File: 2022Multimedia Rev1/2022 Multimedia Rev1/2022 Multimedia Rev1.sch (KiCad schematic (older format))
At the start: 31 parts

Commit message: neatened up schematic
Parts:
- gave numbers to parts that had none: 22
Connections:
- wire segments 86 -> 90
- no-connect marks 0 -> 70
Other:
- moved on the sheet: C3, C6, C7, Conn2, Conn3, Conn4, Conn5, Conn6, R3

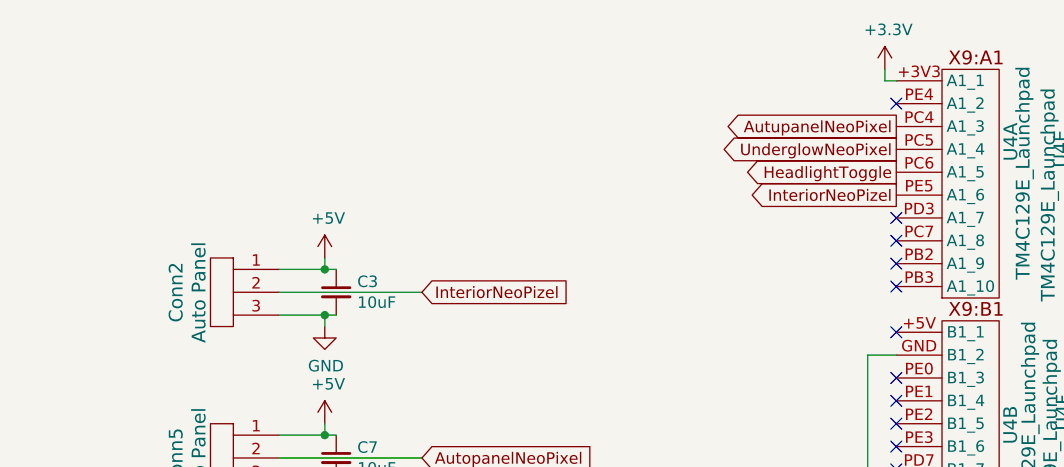
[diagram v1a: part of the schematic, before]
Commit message: Added another neopixel
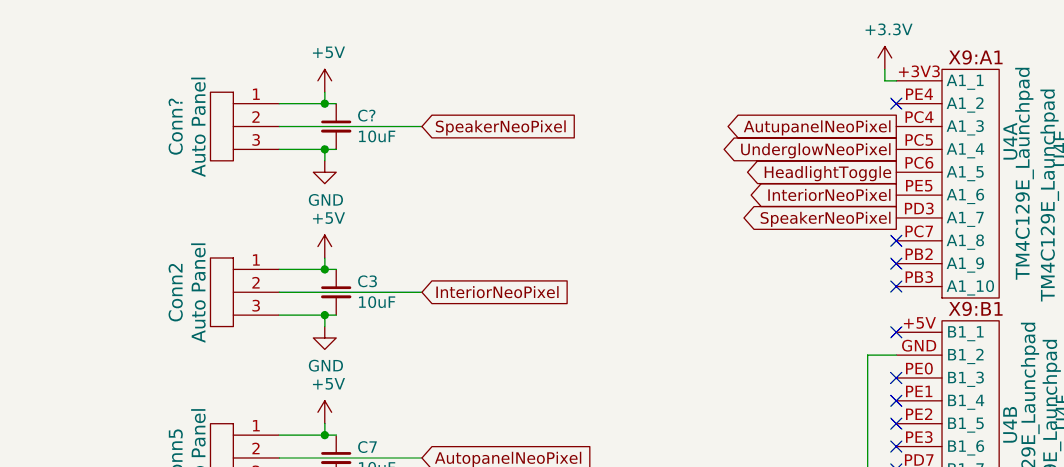
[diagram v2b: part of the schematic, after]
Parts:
- added C?: 10uF, symbol Device:C_Small
- added Conn?: Auto Panel, MRDT_Connectors:MOLEX_uF_S_03_Horizontal, symbol MRDT_Connectors:Molex_uF_S_03
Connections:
- net labels added: InteriorNeoPixel, SpeakerNeoPixel
- net labels removed: InteriorNeoPizel
- wire segments 90 -> 97
- no-connect marks 70 -> 69
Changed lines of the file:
@@
 	6700 1800 6500 1800
 Text GLabel 7125 1900 2    50   Input ~ 0
-InteriorNeoPizel
+InteriorNeoPixel
 Text GLabel 9200 1475 0    50   Output ~ 0
-InteriorNeoPizel
+InteriorNeoPixel
 Wire Wire Line
 	6500 3200 6650 3200
@@
 NoConn ~ 10425 1075
 NoConn ~ 9200 1075
-NoConn ~ 9200 1575
 NoConn ~ 9200 1675
 NoConn ~ 9200 1775
 NoConn ~ 9200 1875
+$Comp
+L MRDT_Connectors:Molex_uF_S_03 Conn?
+U 1 1 6166808D
+P 6300 1325
+F 0 "Conn?" V 6550 1475 60  0000 C CNN
+F 1 "Auto Panel" V 6450 1475 60  0000 C CNN
+F 2 "MRDT_Connectors:MOLEX_uF_S_03_Horizontal" H 6300 1325 60  0001 C CNN
+F 3 "" H 6300 1325 60  0001 C CNN
+	1    6300 1325
+	-1   0    0    -1
+$EndComp
+$Comp
+L Device:C_Small C?
+U 1 1 61668093
+P 6750 1175
+F 0 "C?" H 6842 1221 50  0000 L CNN
+F 1 "10uF" H 6842 1130 50  0000 L CNN
+F 2 "" H 6750 1175 50  0001 C CNN
+F 3 "~" H 6750 1175 50  0001 C CNN
+	1    6750 1175
+	1    0    0    -1
+$EndComp
+$Comp
+L power:GND #PWR?
+U 1 1 61668099
+P 6700 1325
+F 0 "#PWR?" H 6700 1075 50  0001 C CNN
+F 1 "GND" H 6705 1152 50  0000 C CNN
+F 2 "" H 6700 1325 50  0001 C CNN
+F 3 "" H 6700 1325 50  0001 C CNN
+	1    6700 1325
+	1    0    0    -1
+$EndComp
+$Comp
+L power:+5V #PWR?
+U 1 1 6166809F
+P 6700 1025
+F 0 "#PWR?" H 6700 875 50  0001 C CNN
+F 1 "+5V" H 6715 1198 50  0000 C CNN
+F 2 "" H 6700 1025 50  0001 C CNN
+F 3 "" H 6700 1025 50  0001 C CNN
+	1    6700 1025
+	1    0    0    -1
+$EndComp
+Wire Wire Line
+	6700 1325 6700 1275
+Wire Wire Line
+	6500 1275 6700 1275
+Wire Wire Line
+	6750 1075 6700 1075
+Wire Wire Line
+	6700 1025 6700 1075
+Connection ~ 6700 1275
+Wire Wire Line
+	6700 1275 6750 1275
+Connection ~ 6700 1075
+Wire Wire Line
+	6700 1075 6500 1075
+Text GLabel 7125 1175 2    50   Input ~ 0
+SpeakerNeoPixel
+Wire Wire Line
+	6500 1175 7125 1175
+Text GLabel 9200 1575 0    50   Output ~ 0
+SpeakerNeoPixel
 $EndSCHEMATC

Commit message: Fin
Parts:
- R1: value 330 -> 47
- R2: value 480 -> 100
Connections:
- wire segments 97 -> 102
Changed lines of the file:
@@
 P 4750 2875
 F 0 "R1" V 4925 2875 50  0000 C CNN
-F 1 "330" V 4850 2875 50  0000 C CNN
+F 1 "47" V 4850 2875 50  0000 C CNN
 F 2 "" H 4750 2875 50  0001 C CNN
 F 3 "~" H 4750 2875 50  0001 C CNN
@@
 P 4750 3750
 F 0 "R2" V 4925 3750 50  0000 C CNN
-F 1 "480" V 4850 3750 50  0000 C CNN
+F 1 "100" V 4850 3750 50  0000 C CNN
 F 2 "" H 4750 3750 50  0001 C CNN
 F 3 "~" H 4750 3750 50  0001 C CNN
@@
 	9075 4275 9075 4375
 Wire Wire Line
-	9075 2175 9075 4275
-Wire Wire Line
 	9075 2175 9200 2175
 Connection ~ 9075 4275
@@
 Text GLabel 7125 2625 2    50   Input ~ 0
 AutopanelNeoPixel
-Text GLabel 9200 1175 0    50   Output ~ 0
+Text GLabel 8950 2675 0    50   Output ~ 0
 AutupanelNeoPixel
-Text GLabel 9200 1275 0    50   Output ~ 0
+Text GLabel 8950 2775 0    50   Output ~ 0
 UnderglowNeoPixel
-Text GLabel 9200 1375 0    50   Output ~ 0
+Text GLabel 8950 2575 0    50   Output ~ 0
 HeadlightToggle
 $Comp
@@
 Text GLabel 7125 1900 2    50   Input ~ 0
 InteriorNeoPixel
-Text GLabel 9200 1475 0    50   Output ~ 0
+Text GLabel 8950 2975 0    50   Output ~ 0
 InteriorNeoPixel
 Wire Wire Line
@@
 NoConn ~ 9200 2375
 NoConn ~ 9200 2475
-NoConn ~ 9200 2575
-NoConn ~ 9200 2675
-NoConn ~ 9200 2775
-NoConn ~ 9200 2875
-NoConn ~ 9200 2975
 NoConn ~ 10425 1875
 NoConn ~ 10425 1775
@@
 Wire Wire Line
 	6500 1175 7125 1175
-Text GLabel 9200 1575 0    50   Output ~ 0
+Text GLabel 8950 2875 0    50   Output ~ 0
 SpeakerNeoPixel
+NoConn ~ 9200 1175
+NoConn ~ 9200 1275
+NoConn ~ 9200 1375
+NoConn ~ 9200 1475
+NoConn ~ 9200 1575
+Wire Wire Line
+	9075 2175 9075 4275
+Wire Wire Line
+	9200 2575 8950 2575
+Wire Wire Line
+	8950 2675 9200 2675
+Wire Wire Line
+	9200 2775 8950 2775
+Wire Wire Line
+	8950 2875 9200 2875
+Wire Wire Line
+	9200 2975 8950 2975
 $EndSCHEMATC

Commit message: finished layout
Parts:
- C1, C2, C3, C4, C5, C6, C7: footprint (none) -> Capacitor_SMD:C_0603_1608Metric_Pad1.05x0.95mm_HandSolder
- C8: renamed from C?; footprint (none) -> Capacitor_SMD:C_0603_1608Metric_Pad1.05x0.95mm_HandSolder
- Conn1: footprint (none) -> MRDT_Connectors:Anderson_3_Horizontal_Side_by_Side
- Conn2: value Auto Panel -> Interior Lights
- Conn7: renamed from Conn?; value Auto Panel -> Speaker Panel
- D1, D2: footprint (none) -> Diode_SMD:D_0603_1608Metric_Pad1.05x0.95mm_HandSolder
- R1, R2, R3: footprint (none) -> Resistor_SMD:R_0603_1608Metric_Pad1.05x0.95mm_HandSolder
- U1, U2: footprint (none) -> MRDT_Devices:OKI_Horizontal
- U3: footprint (none) -> Package_SO:SOIC-8-1EP_3.9x4.9mm_P1.27mm_EP2.29x3mm
- U4: footprint (none) -> MRDT_Shields:TM4C129E_Launchpad_FULL_SMD_BOTTOM
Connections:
- net labels removed: AutupanelNeoPixel
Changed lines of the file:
@@
 F 0 "U4" V 9701 2523 60  0000 L CNN
 F 1 "TM4C129E_Launchpad" V 9755 2005 60  0000 L CNN
-F 2 "" H 9400 1925 60  0001 C CNN
+F 2 "MRDT_Shields:TM4C129E_Launchpad_FULL_SMD_BOTTOM" H 9400 1925 60  0001 C CNN
 F 3 "" H 9400 1925 60  0001 C CNN
 	1    9400 1925
@@
 F 0 "U4" V 9700 3485 60  0000 L CNN
 F 1 "TM4C129E_Launchpad" V 9780 3090 60  0000 L CNN
-F 2 "" H 9400 3025 60  0001 C CNN
+F 2 "MRDT_Shields:TM4C129E_Launchpad_FULL_SMD_BOTTOM" H 9400 3025 60  0001 C CNN
 F 3 "" H 9400 3025 60  0001 C CNN
 	2    9400 3025
@@
 F 0 "U4" V 9695 4665 60  0000 L CNN
 F 1 "TM4C129E_Launchpad" V 9755 4135 60  0000 L CNN
-F 2 "" H 9400 4125 60  0001 C CNN
+F 2 "MRDT_Shields:TM4C129E_Launchpad_FULL_SMD_BOTTOM" H 9400 4125 60  0001 C CNN
 F 3 "" H 9400 4125 60  0001 C CNN
 	3    9400 4125
@@
 F 0 "U4" V 9695 5765 60  0000 L CNN
 F 1 "TM4C129E_Launchpad" V 9755 5225 60  0000 L CNN
-F 2 "" H 9400 5225 60  0001 C CNN
+F 2 "MRDT_Shields:TM4C129E_Launchpad_FULL_SMD_BOTTOM" H 9400 5225 60  0001 C CNN
 F 3 "" H 9400 5225 60  0001 C CNN
 	4    9400 5225
@@
 F 0 "U4" V 10530 2495 60  0000 L CNN
 F 1 "TM4C129E_Launchpad" V 10585 1910 60  0000 L CNN
-F 2 "" H 10225 1925 60  0001 C CNN
+F 2 "MRDT_Shields:TM4C129E_Launchpad_FULL_SMD_BOTTOM" H 10225 1925 60  0001 C CNN
 F 3 "" H 10225 1925 60  0001 C CNN
 	5    10225 1925
@@
 F 0 "U4" V 10520 3545 60  0000 L CNN
 F 1 "TM4C129E_Launchpad" V 10575 3015 60  0000 L CNN
-F 2 "" H 10225 3025 60  0001 C CNN
+F 2 "MRDT_Shields:TM4C129E_Launchpad_FULL_SMD_BOTTOM" H 10225 3025 60  0001 C CNN
 F 3 "" H 10225 3025 60  0001 C CNN
 	6    10225 3025
@@
 F 0 "U4" V 10525 4770 60  0000 L CNN
 F 1 "TM4C129E_Launchpad" V 10580 4220 60  0000 L CNN
-F 2 "" H 10225 4125 60  0001 C CNN
+F 2 "MRDT_Shields:TM4C129E_Launchpad_FULL_SMD_BOTTOM" H 10225 4125 60  0001 C CNN
 F 3 "" H 10225 4125 60  0001 C CNN
 	7    10225 4125
@@
 F 0 "U4" V 10520 5815 60  0000 L CNN
 F 1 "TM4C129E_Launchpad" V 10570 5275 60  0000 L CNN
-F 2 "" H 10225 5225 60  0001 C CNN
+F 2 "MRDT_Shields:TM4C129E_Launchpad_FULL_SMD_BOTTOM" H 10225 5225 60  0001 C CNN
 F 3 "" H 10225 5225 60  0001 C CNN
 	8    10225 5225
@@
 F 0 "Conn1" H 1500 3900 60  0000 C CNN
 F 1 "AndersonPP" H 1400 3825 60  0000 C CNN
-F 2 "" H 1525 3200 60  0001 C CNN
+F 2 "MRDT_Connectors:Anderson_3_Horizontal_Side_by_Side" H 1525 3200 60  0001 C CNN
 F 3 "" H 1525 3200 60  0001 C CNN
 	1    1675 3750
@@
 F 0 "U1" H 4000 2925 60  0001 C CNN
 F 1 "OKI" H 4150 3256 60  0000 C CNN
-F 2 "" H 3750 2875 60  0001 C CNN
+F 2 "MRDT_Devices:OKI_Horizontal" H 3750 2875 60  0001 C CNN
 F 3 "" H 3750 2875 60  0001 C CNN
 	1    3950 2975
@@
 F 0 "C1" H 3792 3071 50  0000 L CNN
 F 1 "10 uF" H 3792 2980 50  0000 L CNN
-F 2 "" H 3700 3025 50  0001 C CNN
+F 2 "Capacitor_SMD:C_0603_1608Metric_Pad1.05x0.95mm_HandSolder" H 3700 3025 50  0001 C CNN
 F 3 "~" H 3700 3025 50  0001 C CNN
 	1    3700 3025
@@
 F 0 "C4" H 4425 3050 50  0000 L CNN
 F 1 "10 uF" H 4300 2975 50  0000 L CNN
-F 2 "" H 4600 3025 50  0001 C CNN
+F 2 "Capacitor_SMD:C_0603_1608Metric_Pad1.05x0.95mm_HandSolder" H 4600 3025 50  0001 C CNN
 F 3 "~" H 4600 3025 50  0001 C CNN
 	1    4600 3025
@@
 F 0 "R1" V 4925 2875 50  0000 C CNN
 F 1 "47" V 4850 2875 50  0000 C CNN
-F 2 "" H 4750 2875 50  0001 C CNN
+F 2 "Resistor_SMD:R_0603_1608Metric_Pad1.05x0.95mm_HandSolder" H 4750 2875 50  0001 C CNN
 F 3 "~" H 4750 2875 50  0001 C CNN
 	1    4750 2875
@@
 F 0 "D1" H 5043 2620 50  0000 C CNN
 F 1 "Green" H 5043 2711 50  0000 C CNN
-F 2 "" H 5050 2875 50  0001 C CNN
+F 2 "Diode_SMD:D_0603_1608Metric_Pad1.05x0.95mm_HandSolder" H 5050 2875 50  0001 C CNN
 F 3 "~" H 5050 2875 50  0001 C CNN
 	1    5050 2875
@@
 F 0 "U2" H 4000 3800 60  0001 C CNN
 F 1 "OKI" H 4150 4131 60  0000 C CNN
-F 2 "" H 3750 3750 60  0001 C CNN
+F 2 "MRDT_Devices:OKI_Horizontal" H 3750 3750 60  0001 C CNN
 F 3 "" H 3750 3750 60  0001 C CNN
 	1    3950 3850
@@
 F 0 "C2" H 3792 3946 50  0000 L CNN
 F 1 "10 uF" H 3792 3855 50  0000 L CNN
-F 2 "" H 3700 3900 50  0001 C CNN
+F 2 "Capacitor_SMD:C_0603_1608Metric_Pad1.05x0.95mm_HandSolder" H 3700 3900 50  0001 C CNN
 F 3 "~" H 3700 3900 50  0001 C CNN
 	1    3700 3900
@@
 F 0 "C5" H 4425 3925 50  0000 L CNN
 F 1 "10 uF" H 4300 3850 50  0000 L CNN
-F 2 "" H 4600 3900 50  0001 C CNN
+F 2 "Capacitor_SMD:C_0603_1608Metric_Pad1.05x0.95mm_HandSolder" H 4600 3900 50  0001 C CNN
 F 3 "~" H 4600 3900 50  0001 C CNN
 	1    4600 3900
@@
 F 0 "R2" V 4925 3750 50  0000 C CNN
 F 1 "100" V 4850 3750 50  0000 C CNN
-F 2 "" H 4750 3750 50  0001 C CNN
+F 2 "Resistor_SMD:R_0603_1608Metric_Pad1.05x0.95mm_HandSolder" H 4750 3750 50  0001 C CNN
 F 3 "~" H 4750 3750 50  0001 C CNN
 	1    4750 3750
@@
 F 0 "D2" H 5043 3495 50  0000 C CNN
 F 1 "Green" H 5043 3586 50  0000 C CNN
-F 2 "" H 5050 3750 50  0001 C CNN
+F 2 "Diode_SMD:D_0603_1608Metric_Pad1.05x0.95mm_HandSolder" H 5050 3750 50  0001 C CNN
 F 3 "~" H 5050 3750 50  0001 C CNN
 	1    5050 3750
@@
 F 0 "Conn1" H 1500 3650 60  0000 C CNN
 F 1 "AndersonPP" H 1400 3575 60  0000 C CNN
-F 2 "" H 1525 2975 60  0001 C CNN
+F 2 "MRDT_Connectors:Anderson_3_Horizontal_Side_by_Side" H 1525 2975 60  0001 C CNN
 F 3 "" H 1525 2975 60  0001 C CNN
 	3    1675 3525
@@
 F 0 "Conn1" H 1500 3450 60  0000 C CNN
 F 1 "AndersonPP" H 1400 3375 60  0000 C CNN
-F 2 "" H 1525 2750 60  0001 C CNN
+F 2 "MRDT_Connectors:Anderson_3_Horizontal_Side_by_Side" H 1525 2750 60  0001 C CNN
 F 3 "" H 1525 2750 60  0001 C CNN
 	2    1675 3300
@@
 F 0 "C6" H 6800 3400 50  0000 L CNN
 F 1 "10 uF" H 6800 3200 50  0000 L CNN
-F 2 "" H 6700 3300 50  0001 C CNN
+F 2 "Capacitor_SMD:C_0603_1608Metric_Pad1.05x0.95mm_HandSolder" H 6700 3300 50  0001 C CNN
 F 3 "~" H 6700 3300 50  0001 C CNN
 	1    6700 3300
@@
 F 0 "C7" H 6842 2671 50  0000 L CNN
 F 1 "10uF" H 6842 2580 50  0000 L CNN
-F 2 "" H 6750 2625 50  0001 C CNN
+F 2 "Capacitor_SMD:C_0603_1608Metric_Pad1.05x0.95mm_HandSolder" H 6750 2625 50  0001 C CNN
 F 3 "~" H 6750 2625 50  0001 C CNN
 	1    6750 2625
@@
 AutopanelNeoPixel
 Text GLabel 8950 2675 0    50   Output ~ 0
-AutupanelNeoPixel
+AutopanelNeoPixel
 Text GLabel 8950 2775 0    50   Output ~ 0
 UnderglowNeoPixel
@@
 F 0 "R3" H 7143 4696 50  0000 L CNN
 F 1 "480" H 7143 4605 50  0000 L CNN
-F 2 "" H 7075 4650 50  0001 C CNN
+F 2 "Resistor_SMD:R_0603_1608Metric_Pad1.05x0.95mm_HandSolder" H 7075 4650 50  0001 C CNN
 F 3 "~" H 7075 4650 50  0001 C CNN
 	1    7075 4650
@@
 F 0 "U3" H 7500 3825 50  0000 C CNN
 F 1 "BDJ2GA5WEFJ" H 7500 3734 50  0000 C CNN
-F 2 "" H 7475 3950 50  0001 C CNN
+F 2 "Package_SO:SOIC-8-1EP_3.9x4.9mm_P1.27mm_EP2.29x3mm" H 7475 3950 50  0001 C CNN
 F 3 "" H 7475 3950 50  0001 C CNN
 	1    7475 3950
@@
 P 6300 2050
 F 0 "Conn2" V 6550 2200 60  0000 C CNN
-F 1 "Auto Panel" V 6450 2200 60  0000 C CNN
+F 1 "Interior Lights" V 6450 2200 60  0000 C CNN
 F 2 "MRDT_Connectors:MOLEX_uF_S_03_Horizontal" H 6300 2050 60  0001 C CNN
 F 3 "" H 6300 2050 60  0001 C CNN
@@
 F 0 "C3" H 6842 1946 50  0000 L CNN
 F 1 "10uF" H 6842 1855 50  0000 L CNN
-F 2 "" H 6750 1900 50  0001 C CNN
+F 2 "Capacitor_SMD:C_0603_1608Metric_Pad1.05x0.95mm_HandSolder" H 6750 1900 50  0001 C CNN
 F 3 "~" H 6750 1900 50  0001 C CNN
 	1    6750 1900
@@
 NoConn ~ 9200 1875
 $Comp
-L MRDT_Connectors:Molex_uF_S_03 Conn?
+L MRDT_Connectors:Molex_uF_S_03 Conn7
 U 1 1 6166808D
 P 6300 1325
-F 0 "Conn?" V 6550 1475 60  0000 C CNN
-F 1 "Auto Panel" V 6450 1475 60  0000 C CNN
+F 0 "Conn7" V 6550 1475 60  0000 C CNN
+F 1 "Speaker Panel" V 6450 1475 60  0000 C CNN
 F 2 "MRDT_Connectors:MOLEX_uF_S_03_Horizontal" H 6300 1325 60  0001 C CNN
 F 3 "" H 6300 1325 60  0001 C CNN
@@
 $EndComp
 $Comp
-L Device:C_Small C?
+L Device:C_Small C8
 U 1 1 61668093
 P 6750 1175
-F 0 "C?" H 6842 1221 50  0000 L CNN
+F 0 "C8" H 6842 1221 50  0000 L CNN
 F 1 "10uF" H 6842 1130 50  0000 L CNN
-F 2 "" H 6750 1175 50  0001 C CNN
+F 2 "Capacitor_SMD:C_0603_1608Metric_Pad1.05x0.95mm_HandSolder" H 6750 1175 50  0001 C CNN
 F 3 "~" H 6750 1175 50  0001 C CNN
 	1    6750 1175
@@
 $EndComp
 $Comp
-L power:GND #PWR?
+L power:GND #PWR0125
 U 1 1 61668099
 P 6700 1325
-F 0 "#PWR?" H 6700 1075 50  0001 C CNN
+F 0 "#PWR0125" H 6700 1075 50  0001 C CNN
 F 1 "GND" H 6705 1152 50  0000 C CNN
 F 2 "" H 6700 1325 50  0001 C CNN
@@
 $EndComp
 $Comp
-L power:+5V #PWR?
+L power:+5V #PWR0126
 U 1 1 6166809F
 P 6700 1025
-F 0 "#PWR?" H 6700 875 50  0001 C CNN
+F 0 "#PWR0126" H 6700 875 50  0001 C CNN
 F 1 "+5V" H 6715 1198 50  0000 C CNN
 F 2 "" H 6700 1025 50  0001 C CNN

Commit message: changed headlight buck circuit
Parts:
- removed R3: 480, Resistor_SMD:R_0603_1608Metric_Pad1.05x0.95mm_HandSolder, symbol Device:R_Small_US
- added C10, C9: 10 uF, symbol Device:C_Small
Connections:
- wire segments 102 -> 103
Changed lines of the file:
@@
 Text GLabel 7125 2625 2    50   Input ~ 0
 AutopanelNeoPixel
-Text GLabel 8950 2675 0    50   Output ~ 0
+Text GLabel 8950 3175 0    50   Output ~ 0
 AutopanelNeoPixel
-Text GLabel 8950 2775 0    50   Output ~ 0
+Text GLabel 10675 4775 2    50   Output ~ 0
 UnderglowNeoPixel
 Text GLabel 8950 2575 0    50   Output ~ 0
@@
 $EndComp
 $Comp
-L Device:R_Small_US R3
-U 1 1 616E8EA1
-P 7075 4650
-F 0 "R3" H 7143 4696 50  0000 L CNN
-F 1 "480" H 7143 4605 50  0000 L CNN
-F 2 "Resistor_SMD:R_0603_1608Metric_Pad1.05x0.95mm_HandSolder" H 7075 4650 50  0001 C CNN
-F 3 "~" H 7075 4650 50  0001 C CNN
-	1    7075 4650
-	1    0    0    -1
-$EndComp
-$Comp
 L power:GND #PWR0120
 U 1 1 616E8EA7
@@
 Wire Wire Line
 	7125 4500 7075 4500
-Wire Wire Line
-	7075 4500 7075 4550
 $Comp
 L Multimedia~IC:BDJ2GA5WEFJ U3
@@
 L power:+12VA #PWR0121
 U 1 1 616E8EBA
-P 7925 4250
-F 0 "#PWR0121" H 7925 4100 50  0001 C CNN
-F 1 "+12VA" H 7940 4423 50  0000 C CNN
-F 2 "" H 7925 4250 50  0001 C CNN
-F 3 "" H 7925 4250 50  0001 C CNN
-	1    7925 4250
+P 7925 4025
+F 0 "#PWR0121" H 7925 3875 50  0001 C CNN
+F 1 "+12VA" H 7925 4175 50  0000 C CNN
+F 2 "" H 7925 4025 50  0001 C CNN
+F 3 "" H 7925 4025 50  0001 C CNN
+	1    7925 4025
 	1    0    0    -1
 $EndComp
@@
 Wire Wire Line
 	7925 4300 7925 4250
-Wire Wire Line
-	7950 4400 8100 4400
 Connection ~ 7950 4400
 Wire Wire Line
 	6500 3825 6875 3825
-Wire Wire Line
-	8100 3825 8100 4400
 Wire Wire Line
 	6875 4375 6875 3825
@@
 	6500 4375 6875 4375
 Connection ~ 6875 3825
-Wire Wire Line
-	6875 3825 8100 3825
 $Comp
 L power:GND #PWR0122
@@
 Wire Wire Line
 	6650 3925 6775 3925
-Text GLabel 7075 4800 3    50   Input ~ 0
+Text GLabel 7075 4600 3    50   Input ~ 0
 HeadlightToggle
-Wire Wire Line
-	7075 4750 7075 4800
 $Comp
 L MRDT_Connectors:Molex_uF_S_03 Conn2
@@
 Text GLabel 7125 1900 2    50   Input ~ 0
 InteriorNeoPixel
-Text GLabel 8950 2975 0    50   Output ~ 0
+Text GLabel 8975 1075 0    50   Output ~ 0
 InteriorNeoPixel
 Wire Wire Line
@@
 NoConn ~ 10425 4975
 NoConn ~ 10425 4875
-NoConn ~ 10425 4775
 NoConn ~ 10425 4675
 NoConn ~ 10425 4575
@@
 NoConn ~ 9200 4575
 NoConn ~ 9200 4675
-NoConn ~ 9200 4775
 NoConn ~ 9200 4875
 NoConn ~ 9200 4975
@@
 NoConn ~ 10425 3275
 NoConn ~ 10425 3175
-NoConn ~ 9200 3175
 NoConn ~ 9200 3275
 NoConn ~ 9200 3375
@@
 NoConn ~ 10425 1175
 NoConn ~ 10425 1075
-NoConn ~ 9200 1075
 NoConn ~ 9200 1675
 NoConn ~ 9200 1775
@@
 Wire Wire Line
 	6500 1175 7125 1175
-Text GLabel 8950 2875 0    50   Output ~ 0
+Text GLabel 8975 4775 0    50   Output ~ 0
 SpeakerNeoPixel
 NoConn ~ 9200 1175
@@
 	9200 2575 8950 2575
 Wire Wire Line
-	8950 2675 9200 2675
-Wire Wire Line
-	9200 2775 8950 2775
-Wire Wire Line
-	8950 2875 9200 2875
-Wire Wire Line
-	9200 2975 8950 2975
+	7075 4500 7075 4600
+NoConn ~ 9200 2675
+NoConn ~ 9200 2775
+NoConn ~ 9200 2875
+NoConn ~ 9200 2975
+Wire Wire Line
+	10675 4775 10425 4775
+Wire Wire Line
+	9200 4775 8975 4775
+Wire Wire Line
+	9200 3175 8950 3175
+Wire Wire Line
+	9200 1075 8975 1075
+$Comp
+L Device:C_Small C9
+U 1 1 6215CF88
+P 7925 4150
+F 0 "C9" H 8017 4196 50  0000 L CNN
+F 1 "10 uF" H 8017 4105 50  0000 L CNN
+F 2 "" H 7925 4150 50  0001 C CNN
+F 3 "~" H 7925 4150 50  0001 C CNN
+	1    7925 4150
+	1    0    0    -1
+$EndComp
+$Comp
+L Device:C_Small C10
+U 1 1 6215E928
+P 8325 4150
+F 0 "C10" H 8417 4196 50  0000 L CNN
+F 1 "10 uF" H 8417 4105 50  0000 L CNN
+F 2 "" H 8325 4150 50  0001 C CNN
+F 3 "~" H 8325 4150 50  0001 C CNN
+	1    8325 4150
+	1    0    0    -1
+$EndComp
+Wire Wire Line
+	7925 4025 7925 4050
+Wire Wire Line
+	8325 4400 8325 4250
+Wire Wire Line
+	7950 4400 8325 4400
+Wire Wire Line
+	8325 4050 8325 3825
+Wire Wire Line
+	6875 3825 8325 3825
 $EndSCHEMATC

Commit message: Rev2 Done
Need to do Gerbs
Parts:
- removed C3, C8: 10uF, Capacitor_SMD:C_0603_1608Metric_Pad1.05x0.95mm_HandSolder, symbol Device:C_Small
- removed C6: 10 uF, Capacitor_SMD:C_0603_1608Metric_Pad1.05x0.95mm_HandSolder, symbol Device:C_Small
- removed Conn2: Interior Lights, MRDT_Connectors:MOLEX_uF_S_03_Horizontal, symbol MRDT_Connectors:Molex_uF_S_03
- removed Conn3: Lights, MRDT_Connectors:MOLEX_uF_S_02_Horizontal, symbol MRDT_Connectors:Molex_uF_S_02
- removed Conn4: Lights2, MRDT_Connectors:MOLEX_uF_S_02_Horizontal, symbol MRDT_Connectors:Molex_uF_S_02
- removed Conn6: Underglow, MRDT_Connectors:MOLEX_uF_S_03_Horizontal, symbol MRDT_Connectors:Molex_uF_S_03
- removed Conn7: Speaker Panel, MRDT_Connectors:MOLEX_uF_S_03_Horizontal, symbol MRDT_Connectors:Molex_uF_S_03
- added Conn2: Wirrly Light, MRDT_Connectors:Square_Anderson_2_H_Side_By_Side, symbol MRDT_Connectors:AndersonPP
- added Conn3: Headlight, MRDT_Connectors:Square_Anderson_2_H_Side_By_Side, symbol MRDT_Connectors:AndersonPP
- C10, C9: footprint (none) -> Capacitor_SMD:C_0603_1608Metric_Pad1.05x0.95mm_HandSolder
- Conn1: footprint MRDT_Connectors:Anderson_3_Horizontal_Side_by_Side -> MRDT_Connectors:Square_Anderson_3_H_Side_By_Side
- R1: value 47 -> 120
- R2: value 100 -> 300
- U3: symbol Multimedia~IC:BDJ2GA5WEFJ -> Multimedia_IC:BDJ2GA5WEFJ
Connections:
- net labels removed: InteriorNeoPixel, SpeakerNeoPixel, UnderglowNeoPixel
- wire segments 103 -> 85
- no-connect marks 69 -> 72
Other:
- moved on the sheet: C10, C9
